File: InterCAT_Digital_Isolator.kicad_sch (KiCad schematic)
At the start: 21 parts, among them U10 MAX3250, U11 TLP185, U12 TLP185, U8 TLP185, U9 TLP185

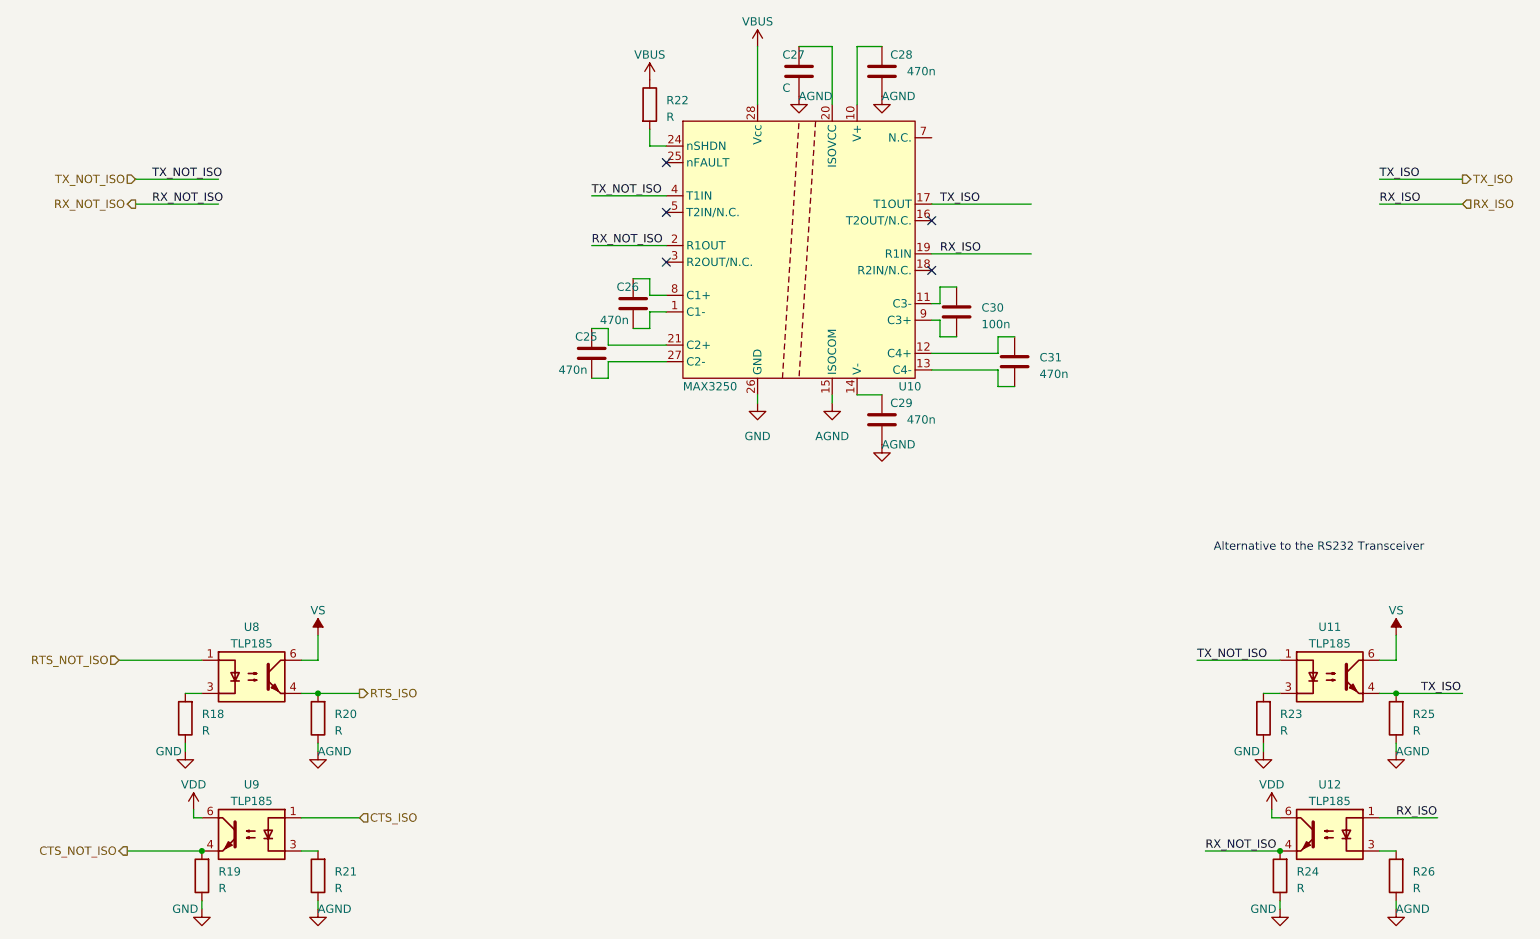
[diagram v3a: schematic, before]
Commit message: changed optocouplers, started compiling BOM
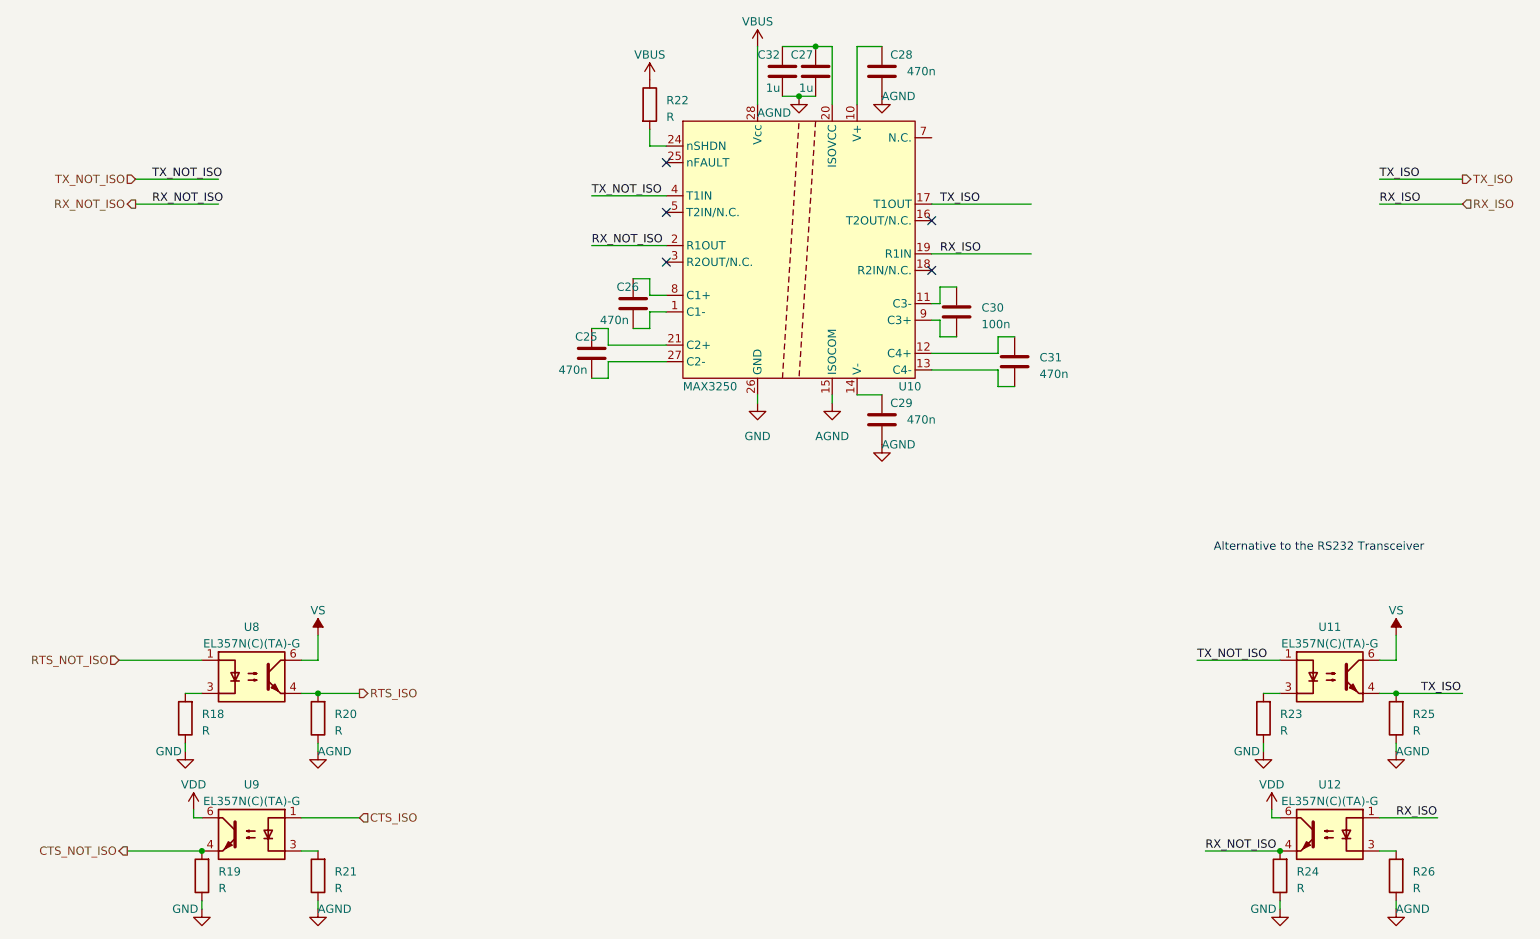
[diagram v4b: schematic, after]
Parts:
- added C32: 1u, Capacitor_SMD:C_0805_2012Metric, symbol Device:C
- C25, C26, C28, C29, C31: footprint Capacitor_SMD:C_0603_1608Metric -> Capacitor_SMD:C_0402_1005Metric
- C27: value C -> 1u; footprint Capacitor_SMD:C_0603_1608Metric -> Capacitor_SMD:C_0805_2012Metric; LCSC (none) -> C28323; Note (none) -> X7R
- C30: LCSC (none) -> C14663; Note (none) -> X7R
- U11, U12, U8, U9: value TLP185 -> EL357N(C)(TA)-G; footprint Package_SO:SOIC-4_4.55x3.7mm_P2.54mm -> Package_SO:SO-4_4.4x3.9mm_P2.54mm; LCSC (none) -> C29981
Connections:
- net GNDA: now also C32.2
- net at C27.1, U10.20 (ISOVCC): now also C32.1
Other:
- moved on the sheet: C27

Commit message: continuation on BOM
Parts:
- C25, C26, C28, C29, C31: LCSC (none) -> C1623; Note (none) -> 25V X7R
- R18, R19, R20, R21, R22, R23, R24, R25, R26: value R -> 1k; LCSC (none) -> C21190
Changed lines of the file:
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@@
       (effects (font (size 1.27 1.27)) hide)
     )
-    (property "LCSC" "" (at 127 66.04 0)
-      (effects (font (size 1.27 1.27)) hide)
-    )
-    (property "Note" "" (at 127 66.04 0)
+    (property "LCSC" "C1623" (at 127 66.04 0)
+      (effects (font (size 1.27 1.27)) hide)
+    )
+    (property "Note" "25V X7R" (at 127 66.04 0)
       (effects (font (size 1.27 1.27)) hide)
     )
@@
       (effects (font (size 1.27 1.27)) (justify right))
     )
-    (property "Value" "R" (at 60.96 131.445 0)
+    (property "Value" "1k" (at 60.96 131.445 0)
       (effects (font (size 1.27 1.27)) (justify right))
     )
@@
       (effects (font (size 1.27 1.27)) hide)
     )
-    (property "LCSC" "" (at 58.42 129.54 0)
+    (property "LCSC" "C21190" (at 58.42 129.54 0)
       (effects (font (size 1.27 1.27)) hide)
     )
@@
       (effects (font (size 1.27 1.27)) (justify right))
     )
-    (property "Value" "R" (at 81.28 155.575 0)
+    (property "Value" "1k" (at 81.28 155.575 0)
       (effects (font (size 1.27 1.27)) (justify right))
     )
@@
       (effects (font (size 1.27 1.27)) hide)
     )
-    (property "LCSC" "" (at 78.74 153.67 0)
+    (property "LCSC" "C21190" (at 78.74 153.67 0)
       (effects (font (size 1.27 1.27)) hide)
     )
@@
       (effects (font (size 1.27 1.27)) (justify right))
     )
-    (property "Value" "R" (at 246.38 131.445 0)
+    (property "Value" "1k" (at 246.38 131.445 0)
       (effects (font (size 1.27 1.27)) (justify right))
     )
@@
       (effects (font (size 1.27 1.27)) hide)
     )
-    (property "LCSC" "" (at 243.84 129.54 0)
+    (property "LCSC" "C21190" (at 243.84 129.54 0)
       (effects (font (size 1.27 1.27)) hide)
     )
@@
       (effects (font (size 1.27 1.27)) hide)
     )
-    (property "LCSC" "" (at 185.42 74.93 0)
-      (effects (font (size 1.27 1.27)) hide)
-    )
-    (property "Note" "" (at 185.42 74.93 0)
+    (property "LCSC" "C1623" (at 185.42 74.93 0)
+      (effects (font (size 1.27 1.27)) hide)
+    )
+    (property "Note" "25V X7R" (at 185.42 74.93 0)
       (effects (font (size 1.27 1.27)) hide)
     )
@@
       (effects (font (size 1.27 1.27)) (justify right))
     )
-    (property "Value" "R" (at 81.28 131.445 0)
+    (property "Value" "1k" (at 81.28 131.445 0)
       (effects (font (size 1.27 1.27)) (justify right))
     )
@@
       (effects (font (size 1.27 1.27)) hide)
     )
-    (property "LCSC" "" (at 78.74 129.54 0)
+    (property "LCSC" "C21190" (at 78.74 129.54 0)
       (effects (font (size 1.27 1.27)) hide)
     )
@@
       (effects (font (size 1.27 1.27)) (justify right))
     )
-    (property "Value" "R" (at 228.6 155.575 0)
+    (property "Value" "1k" (at 228.6 155.575 0)
       (effects (font (size 1.27 1.27)) (justify right))
     )
@@
       (effects (font (size 1.27 1.27)) hide)
     )
-    (property "LCSC" "" (at 226.06 153.67 0)
+    (property "LCSC" "C21190" (at 226.06 153.67 0)
       (effects (font (size 1.27 1.27)) hide)
     )
@@
       (effects (font (size 1.27 1.27)) (justify right))
     )
-    (property "Value" "R" (at 246.38 155.575 0)
+    (property "Value" "1k" (at 246.38 155.575 0)
       (effects (font (size 1.27 1.27)) (justify right))
     )
@@
       (effects (font (size 1.27 1.27)) hide)
     )
-    (property "LCSC" "" (at 243.84 153.67 0)
+    (property "LCSC" "C21190" (at 243.84 153.67 0)
       (effects (font (size 1.27 1.27)) hide)
     )
@@
       (effects (font (size 1.27 1.27)) hide)
     )
-    (property "LCSC" "" (at 165.1 30.48 0)
-      (effects (font (size 1.27 1.27)) hide)
-    )
-    (property "Note" "" (at 165.1 30.48 0)
+    (property "LCSC" "C1623" (at 165.1 30.48 0)
+      (effects (font (size 1.27 1.27)) hide)
+    )
+    (property "Note" "25V X7R" (at 165.1 30.48 0)
       (effects (font (size 1.27 1.27)) hide)
     )
@@
       (effects (font (size 1.27 1.27)) hide)
     )
-    (property "LCSC" "" (at 120.65 73.66 0)
-      (effects (font (size 1.27 1.27)) hide)
-    )
-    (property "Note" "" (at 120.65 73.66 0)
+    (property "LCSC" "C1623" (at 120.65 73.66 0)
+      (effects (font (size 1.27 1.27)) hide)
+    )
+    (property "Note" "25V X7R" (at 120.65 73.66 0)
       (effects (font (size 1.27 1.27)) hide)
     )
@@
       (effects (font (size 1.27 1.27)) (justify left))
     )
-    (property "Value" "R" (at 132.08 37.465 0)
+    (property "Value" "1k" (at 132.08 37.465 0)
       (effects (font (size 1.27 1.27)) (justify left))
     )
@@
       (effects (font (size 1.27 1.27)) hide)
     )
-    (property "LCSC" "" (at 129.54 35.56 0)
+    (property "LCSC" "C21190" (at 129.54 35.56 0)
       (effects (font (size 1.27 1.27)) hide)
     )
@@
       (effects (font (size 1.27 1.27)) (justify right))
     )
-    (property "Value" "R" (at 63.5 155.575 0)
+    (property "Value" "1k" (at 63.5 155.575 0)
       (effects (font (size 1.27 1.27)) (justify right))
     )
@@
       (effects (font (size 1.27 1.27)) hide)
     )
-    (property "LCSC" "" (at 60.96 153.67 0)
+    (property "LCSC" "C21190" (at 60.96 153.67 0)
       (effects (font (size 1.27 1.27)) hide)
     )
@@
       (effects (font (size 1.27 1.27)) (justify right))
     )
-    (property "Value" "R" (at 226.06 131.445 0)
+    (property "Value" "1k" (at 226.06 131.445 0)
       (effects (font (size 1.27 1.27)) (justify right))
     )
@@
       (effects (font (size 1.27 1.27)) hide)
     )
-    (property "LCSC" "" (at 223.52 129.54 0)
+    (property "LCSC" "C21190" (at 223.52 129.54 0)
       (effects (font (size 1.27 1.27)) hide)
     )
@@
       (effects (font (size 1.27 1.27)) hide)
     )
-    (property "LCSC" "" (at 165.1 83.82 0)
-      (effects (font (size 1.27 1.27)) hide)
-    )
-    (property "Note" "" (at 165.1 83.82 0)
-      (effects (font (size 1.27 1.27)) hide)
-    )
+    (property "LCSC" "C1623" (at 165.1 83.82 0)
+      (effects (font (size 1.27 1.27)) hide)
+    )
+    (property "Note" "25V X7R" (at 165.1 83.82 0)
+      (effects (font (size 1.27 1.27)) hide)
+    )

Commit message: completed JLC BOM and changed DB9
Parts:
- U10: LCSC (none) -> C2671045
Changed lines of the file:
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@@
       (effects (font (size 1.27 1.27)) hide)
     )
-    (property "LCSC" "" (at 152.4 62.23 0)
+    (property "LCSC" "C2671045" (at 152.4 62.23 0)
       (effects (font (size 1.27 1.27)) hide)
     )

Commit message: added edge cuts, smaller PCB, bugfix
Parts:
- C25, C26, C28, C29, C31: footprint Capacitor_SMD:C_0402_1005Metric -> Capacitor_SMD:C_0603_1608Metric
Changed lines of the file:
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@@
       (effects (font (size 1.27 1.27)) (justify left))
     )
-    (property "Footprint" "Capacitor_SMD:C_0402_1005Metric" (at 127.9652 69.85 0)
+    (property "Footprint" "Capacitor_SMD:C_0603_1608Metric" (at 127.9652 69.85 0)
       (effects (font (size 1.27 1.27)) hide)
     )
@@
       (effects (font (size 1.27 1.27)) (justify left))
     )
-    (property "Footprint" "Capacitor_SMD:C_0402_1005Metric" (at 186.3852 78.74 0)
+    (property "Footprint" "Capacitor_SMD:C_0603_1608Metric" (at 186.3852 78.74 0)
       (effects (font (size 1.27 1.27)) hide)
     )
@@
       (effects (font (size 1.27 1.27)) (justify left))
     )
-    (property "Footprint" "Capacitor_SMD:C_0402_1005Metric" (at 166.0652 34.29 0)
+    (property "Footprint" "Capacitor_SMD:C_0603_1608Metric" (at 166.0652 34.29 0)
       (effects (font (size 1.27 1.27)) hide)
     )
@@
       (effects (font (size 1.27 1.27)) (justify left))
     )
-    (property "Footprint" "Capacitor_SMD:C_0402_1005Metric" (at 121.6152 77.47 0)
+    (property "Footprint" "Capacitor_SMD:C_0603_1608Metric" (at 121.6152 77.47 0)
       (effects (font (size 1.27 1.27)) hide)
     )
@@
       (effects (font (size 1.27 1.27)) (justify left))
     )
-    (property "Footprint" "Capacitor_SMD:C_0402_1005Metric" (at 166.0652 87.63 0)
-      (effects (font (size 1.27 1.27)) hide)
-    )
+    (property "Footprint" "Capacitor_SMD:C_0603_1608Metric" (at 166.0652 87.63 0)
+      (effects (font (size 1.27 1.27)) hide)
+    )

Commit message: reduced PCB size, started routing
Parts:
- U11, U12, U8, U9: footprint Package_SO:SO-4_4.4x3.9mm_P2.54mm -> InterCat:SO-6-4_4.4x3.9mm_P2.54mm
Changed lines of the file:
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@@
       (effects (font (size 1.27 1.27)))
     )
-    (property "Footprint" "Package_SO:SO-4_4.4x3.9mm_P2.54mm" (at 233.68 154.94 0)
+    (property "Footprint" "InterCat:SO-6-4_4.4x3.9mm_P2.54mm" (at 233.68 154.94 0)
       (effects (font (size 1.27 1.27) italic) hide)
     )
@@
       (effects (font (size 1.27 1.27)))
     )
-    (property "Footprint" "Package_SO:SO-4_4.4x3.9mm_P2.54mm" (at 68.58 130.81 0)
+    (property "Footprint" "InterCat:SO-6-4_4.4x3.9mm_P2.54mm" (at 68.58 130.81 0)
       (effects (font (size 1.27 1.27) italic) hide)
     )
@@
       (effects (font (size 1.27 1.27)))
     )
-    (property "Footprint" "Package_SO:SO-4_4.4x3.9mm_P2.54mm" (at 233.68 130.81 0)
+    (property "Footprint" "InterCat:SO-6-4_4.4x3.9mm_P2.54mm" (at 233.68 130.81 0)
       (effects (font (size 1.27 1.27) italic) hide)
     )
@@
       (effects (font (size 1.27 1.27)))
     )
-    (property "Footprint" "Package_SO:SO-4_4.4x3.9mm_P2.54mm" (at 68.58 154.94 0)
+    (property "Footprint" "InterCat:SO-6-4_4.4x3.9mm_P2.54mm" (at 68.58 154.94 0)
       (effects (font (size 1.27 1.27) italic) hide)
     )
